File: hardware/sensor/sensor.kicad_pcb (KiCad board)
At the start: 2 copper layers, 25.7 x 45.5 mm, 49 parts, among them P1 CONN_01X05, SW1 Reset, T1 BUK9Y22, T2 DMP10H4D2s, U1 LMR16006, U2 OPA376AIDCK, U3 CD74HC4046, U5 Atmel_SAM_D09, X1 60V, X2 UART

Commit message: soo eigentlich gloub ke grossi änderige...
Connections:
- X2 pad : (no net) -> GND
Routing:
- net GND: track 92.3 -> 101.2 mm
- net (no net): track 0.00 -> 0.59 mm, vias 0 -> 1
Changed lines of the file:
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@@
   (general
     (links 157)
-    (no_connects 49)
-    (area 126.949999 54.051999 152.704001 99.618001)
+    (no_connects 47)
+    (area 122.153286 45.639999 152.704001 101.743)
     (thickness 1.6)
     (drawings 5)
-    (tracks 399)
+    (tracks 412)
     (zones 0)
     (modules 49)
@@
       (net 2 GND))
     (pad "" smd rect (at -4.425 0 90) (size 2.1 3) (layers B.Cu B.Paste B.Mask))
-    (pad "" smd rect (at 4.425 0 90) (size 2.1 3) (layers B.Cu B.Paste B.Mask))
+    (pad "" smd rect (at 4.425 0 90) (size 2.1 3) (layers B.Cu B.Paste B.Mask)
+      (net 2 GND))
   )
   (module LEDs:LED_0603 (layer B.Cu)
@@
   (gr_line (start 152.654 54.102) (end 152.654 99.568) (angle 90) (layer Edge.Cuts) (width 0.1))
   (gr_line (start 127 54.102) (end 152.654 54.102) (angle 90) (layer Edge.Cuts) (width 0.1))
+  (segment (start 146.292231 56.702127) (end 146.162289 56.572185) (width 0.4) (layer F.Cu) (net 0))
+  (segment (start 146.698298 56.702127) (end 146.292231 56.702127) (width 0.4) (layer F.Cu) (net 0))
+  (via (at 146.162289 56.572185) (size 1.3) (drill 0.9) (layers F.Cu B.Cu) (net 0))
   (segment (start 133.67004 65.024) (end 133.67004 63.52704) (width 0.4) (layer F.Cu) (net 1))
   (segment (start 133.67004 63.52704) (end 133.643 63.5) (width 0.4) (layer F.Cu) (net 1))
@@
   (segment (start 133.643 62.572) (end 134.62 61.595) (width 0.4) (layer F.Cu) (net 1))
   (segment (start 132.075 61.595) (end 134.62 61.595) (width 0.4) (layer F.Cu) (net 1))
+  (segment (start 131.944 74.676) (end 133.35 74.676) (width 0.4) (layer B.Cu) (net 2))
+  (segment (start 131.932 74.688) (end 131.944 74.676) (width 0.4) (layer B.Cu) (net 2))
+  (segment (start 131.932 75.488) (end 131.932 74.688) (width 0.4) (layer B.Cu) (net 2))
+  (segment (start 131.932 75.488) (end 132.538 75.488) (width 0.4) (layer B.Cu) (net 2))
+  (segment (start 131.932 75.488) (end 133.554 75.488) (width 0.4) (layer B.Cu) (net 2))
+  (via (at 134.366 74.676) (size 1.3) (drill 0.9) (layers F.Cu B.Cu) (net 2))
+  (segment (start 133.554 75.488) (end 134.366 74.676) (width 0.4) (layer B.Cu) (net 2))
+  (segment (start 139.167 81.026) (end 139.167 81.237011) (width 0.4) (layer B.Cu) (net 2))
+  (segment (start 139.167 81.237011) (end 138.196224 82.207787) (width 0.4) (layer B.Cu) (net 2))
+  (segment (start 138.196224 82.207787) (end 138.196224 82.45362) (width 0.4) (layer B.Cu) (net 2))
+  (segment (start 139.192 81.026) (end 139.192 81.282249) (width 0.25) (layer B.Cu) (net 2))
+  (segment (start 139.192 81.282249) (end 138.176 82.298249) (width 0.25) (layer B.Cu) (net 2))
+  (segment (start 138.176 82.298249) (end 138.176 82.667) (width 0.25) (layer B.Cu) (net 2))
   (segment (start 134.62 82.538) (end 134.378 82.538) (width 0.4) (layer B.Cu) (net 2))
   (segment (start 134.378 82.538) (end 133.604 83.312) (width 0.4) (layer B.Cu) (net 2))
@@
   (segment (start 129.54 56.515) (end 129.54 58.652966) (width 0.4) (layer B.Cu) (net 2))
   (segment (start 129.54 58.652966) (end 129.259483 58.933483) (width 0.4) (layer B.Cu) (net 2))
-  (segment (start 146.292231 56.702127) (end 146.162289 56.572185) (width 0.4) (layer F.Cu) (net 2))
-  (segment (start 146.698298 56.702127) (end 146.292231 56.702127) (width 0.4) (layer F.Cu) (net 2))
-  (via (at 146.162289 56.572185) (size 1.3) (drill 0.9) (layers F.Cu B.Cu) (net 2))
   (segment (start 139.434 87.63) (end 141.224 87.63) (width 0.25) (layer B.Cu) (net 2))
   (segment (start 141.224 87.63) (end 141.732 88.138) (width 0.25) (layer B.Cu) (net 2))
@@
   (segment (start 129.54 60.96) (end 130.175 61.595) (width 0.25) (layer F.Cu) (net 12))
   (segment (start 131.509 63.524) (end 131.533 63.5) (width 0.25) (layer F.Cu) (net 12))
+  (segment (start 140.966 79.166) (end 140.966 81.339312) (width 0.25) (layer B.Cu) (net 13))
+  (segment (start 140.099479 83.250624) (end 141.006852 84.157997) (width 0.25) (layer B.Cu) (net 13))
+  (segment (start 140.966 81.339312) (end 140.099479 82.205833) (width 0.25) (layer B.Cu) (net 13))
+  (segment (start 140.099479 82.205833) (end 140.099479 83.250624) (width 0.25) (layer B.Cu) (net 13))
+  (segment (start 141.006852 84.157997) (end 143.593997 84.157997) (width 0.25) (layer B.Cu) (net 13))
   (segment (start 150.528775 61.582876) (end 150.528775 62.502114) (width 0.4) (layer F.Cu) (net 13))
+  (segment (start 143.523001 84.157997) (end 147.006931 80.674067) (width 0.3) (layer B.Cu) (net 13))
+  (via (at 150.528775 62.502114) (size 1.3) (drill 0.9) (layers F.Cu B.Cu) (net 13))
+  (segment (start 147.006931 80.674067) (end 150.528775 77.152223) (width 0.3) (layer B.Cu) (net 13))
+  (segment (start 150.528775 77.152223) (end 150.528775 63.421352) (width 0.3) (layer B.Cu) (net 13))
+  (segment (start 150.528775 59.696775) (end 150.528775 61.582876) (width 0.4) (layer F.Cu) (net 13))
+  (segment (start 150.528775 63.421352) (end 150.528775 62.502114) (width 0.3) (layer B.Cu) (net 13))
+  (segment (start 149.086 57.404) (end 149.086 58.254) (width 0.4) (layer F.Cu) (net 13))
   (segment (start 149.086 58.254) (end 150.528775 59.696775) (width 0.4) (layer F.Cu) (net 13))
-  (segment (start 149.086 57.404) (end 149.086 58.254) (width 0.4) (layer F.Cu) (net 13))
-  (segment (start 150.528775 63.421352) (end 150.528775 62.502114) (width 0.3) (layer B.Cu) (net 13))
-  (segment (start 150.528775 59.696775) (end 150.528775 61.582876) (width 0.4) (layer F.Cu) (net 13))
-  (segment (start 150.528775 77.152223) (end 150.528775 63.421352) (width 0.3) (layer B.Cu) (net 13))
-  (segment (start 147.006931 80.674067) (end 150.528775 77.152223) (width 0.3) (layer B.Cu) (net 13))
-  (via (at 150.528775 62.502114) (size 1.3) (drill 0.9) (layers F.Cu B.Cu) (net 13))
   (segment (start 145.542 88.646) (end 145.542 91.036) (width 0.4) (layer F.Cu) (net 13))
   (segment (start 145.542 91.036) (end 145.535 91.043) (width 0.4) (layer F.Cu) (net 13))
@@
   (segment (start 145.542 86.106) (end 145.542 88.646) (width 0.4) (layer B.Cu) (net 13))
   (via (at 145.542 88.646) (size 1.3) (drill 0.9) (layers F.Cu B.Cu) (net 13))
-  (segment (start 143.523001 84.157997) (end 143.593997 84.157997) (width 0.4) (layer B.Cu) (net 13))
-  (segment (start 143.523001 84.157997) (end 147.006931 80.674067) (width 0.3) (layer B.Cu) (net 13))
-  (segment (start 140.966 79.166) (end 140.966 81.418762) (width 0.3) (layer B.Cu) (net 13))
-  (segment (start 139.683853 82.700909) (end 141.14094 84.157997) (width 0.3) (layer B.Cu) (net 13))
-  (segment (start 140.966 81.418762) (end 139.683853 82.700909) (width 0.3) (layer B.Cu) (net 13))
-  (segment (start 141.14094 84.157997) (end 143.523001 84.157997) (width 0.3) (layer B.Cu) (net 13))
   (segment (start 134.62 65.024) (end 134.62 64.99) (width 0.4) (layer F.Cu) (net 14))
   (segment (start 134.62 64.99) (end 135.094 64.516) (width 0.4) (layer F.Cu) (net 14))
@@
   (segment (start 143.764 57.912) (end 143.256 57.912) (width 0.25) (layer F.Cu) (net 18))
   (segment (start 143.256 57.912) (end 142.24 58.928) (width 0.25) (layer F.Cu) (net 18))
-  (segment (start 140.466 79.166) (end 140.466 81.017357) (width 0.25) (layer B.Cu) (net 19))
-  (segment (start 140.466 81.017357) (end 138.948786 82.534571) (width 0.25) (layer B.Cu) (net 19))
-  (segment (start 139.735427 94.996) (end 138.733 94.996) (width 0.25) (layer B.Cu) (net 19))
-  (segment (start 138.948786 82.534571) (end 138.948786 83.194299) (width 0.25) (layer B.Cu) (net 19))
-  (segment (start 143.224212 87.469826) (end 143.224212 88.662786) (width 0.25) (layer B.Cu) (net 19))
-  (segment (start 138.948786 83.194299) (end 142.521474 86.766987) (width 0.25) (layer B.Cu) (net 19))
-  (segment (start 142.521474 86.766987) (end 142.521474 86.767088) (width 0.25) (layer B.Cu) (net 19))
+  (segment (start 140.466 79.166) (end 140.466 81.101811) (width 0.25) (layer B.Cu) (net 19))
+  (segment (start 140.466 81.101811) (end 139.460312 82.107499) (width 0.25) (layer B.Cu) (net 19))
+  (segment (start 139.460312 82.107499) (end 139.460312 83.705825) (width 0.25) (layer B.Cu) (net 19))
+  (segment (start 138.733 94.996) (end 137.59 93.853) (width 0.25) (layer B.Cu) (net 19))
+  (segment (start 139.460312 83.705825) (end 142.521474 86.766987) (width 0.25) (layer B.Cu) (net 19))
   (segment (start 142.521474 86.767088) (end 143.224212 87.469826) (width 0.25) (layer B.Cu) (net 19))
   (segment (start 143.224212 88.662786) (end 141.951999 89.934999) (width 0.25) (layer B.Cu) (net 19))
+  (segment (start 141.951999 92.779428) (end 139.735427 94.996) (width 0.25) (layer B.Cu) (net 19))
+  (segment (start 142.521474 86.766987) (end 142.521474 86.767088) (width 0.25) (layer B.Cu) (net 19))
+  (segment (start 137.59 93.853) (end 137.565 93.853) (width 0.25) (layer B.Cu) (net 19))
+  (segment (start 143.224212 87.469826) (end 143.224212 88.662786) (width 0.25) (layer B.Cu) (net 19))
   (segment (start 141.951999 89.934999) (end 141.951999 92.779428) (width 0.25) (layer B.Cu) (net 19))
-  (segment (start 141.951999 92.779428) (end 139.735427 94.996) (width 0.25) (layer B.Cu) (net 19))
-  (segment (start 138.733 94.996) (end 137.59 93.853) (width 0.25) (layer B.Cu) (net 19))
-  (segment (start 137.59 93.853) (end 137.565 93.853) (width 0.25) (layer B.Cu) (net 19))
+  (segment (start 139.735427 94.996) (end 138.733 94.996) (width 0.25) (layer B.Cu) (net 19))
   (segment (start 136.271 93.98) (end 137.438 93.98) (width 0.4) (layer B.Cu) (net 19))
   (segment (start 137.438 93.98) (end 137.565 93.853) (width 0.4) (layer B.Cu) (net 19))
@@
     (min_thickness 0.254)
     (keepout (tracks not_allowed) (vias not_allowed) (copperpour not_allowed))
-    (fill yes (arc_segments 16) (thermal_gap 0.508) (thermal_bridge_width 0.508))
+    (fill (arc_segments 16) (thermal_gap 0.508) (thermal_bridge_width 0.508))
     (polygon
       (pts
-        (xy 127.381 74.295) (xy 130.683 74.295) (xy 130.683 80.264) (xy 127.381 80.264)
+        (xy 127.381 74.295) (xy 130.937 74.295) (xy 130.937 80.264) (xy 127.381 80.264)
       )
     )

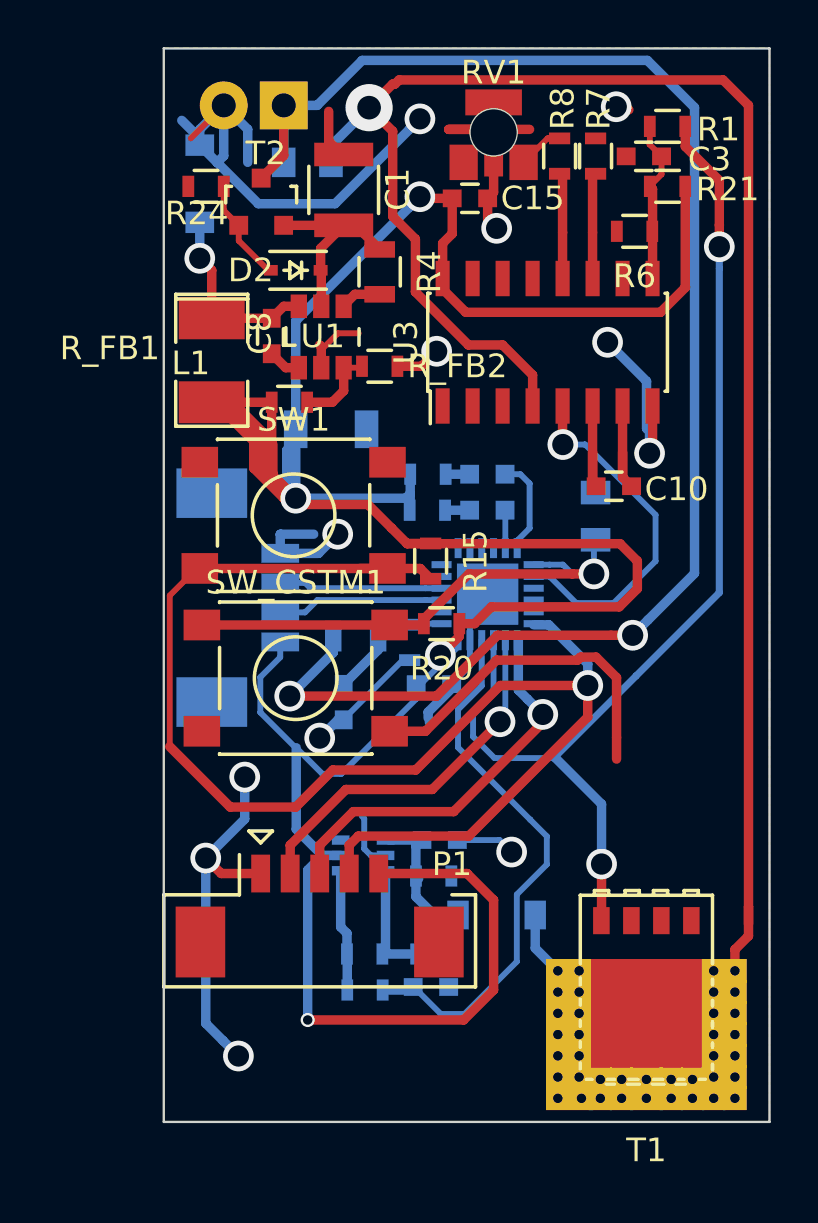
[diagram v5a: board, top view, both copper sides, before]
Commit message: Sensor fixes
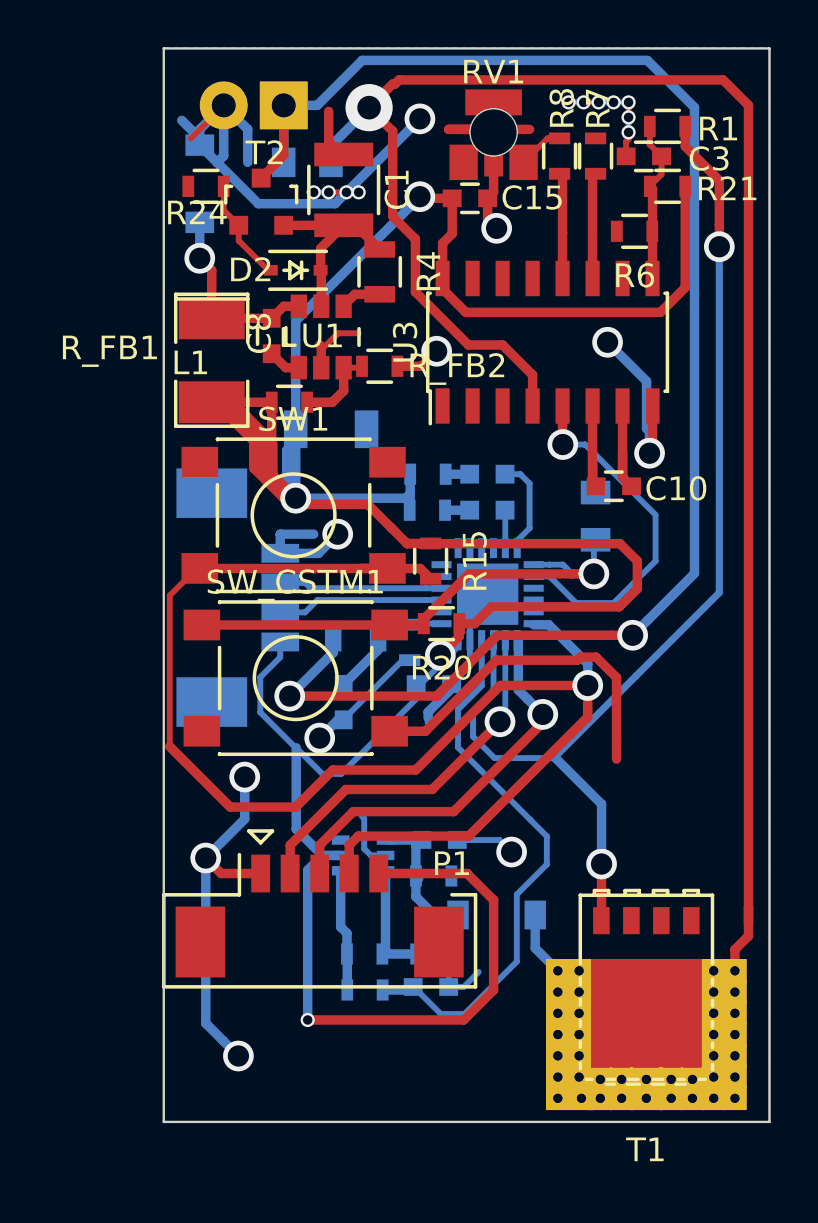
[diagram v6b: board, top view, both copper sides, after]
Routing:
- net GND: track 101.2 -> 110.9 mm, vias 11 -> 22
- net (no net): track 0.59 -> 0.00 mm, vias 1 -> 0
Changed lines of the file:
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@@
-(kicad_pcb (version 4) (host pcbnew "(2015-09-15 BZR 6201)-product")
+(kicad_pcb (version 4) (host pcbnew 4.0.2-stable)
   (general
-    (links 157)
-    (no_connects 47)
+    (links 158)
+    (no_connects 43)
     (area 122.153286 45.639999 152.704001 101.743)
     (thickness 1.6)
     (drawings 5)
-    (tracks 412)
+    (tracks 438)
     (zones 0)
     (modules 49)
@@
   )
   (setup
-    (last_trace_width 0.4)
+    (last_trace_width 0.25)
     (user_trace_width 0.4)
     (trace_clearance 0.2)
@@
     (aux_axis_origin 0 0)
     (grid_origin 127 99.568)
-    (visible_elements FFFFFF7F)
+    (visible_elements 7FFFFFFF)
     (pcbplotparams
-      (layerselection 0x01000_80000001)
+      (layerselection 0x010f0_80000001)
       (usegerberextensions false)
       (excludeedgelayer true)
@@
   (gr_line (start 152.654 54.102) (end 152.654 99.568) (angle 90) (layer Edge.Cuts) (width 0.1))
   (gr_line (start 127 54.102) (end 152.654 54.102) (angle 90) (layer Edge.Cuts) (width 0.1))
-  (segment (start 146.292231 56.702127) (end 146.162289 56.572185) (width 0.4) (layer F.Cu) (net 0))
-  (segment (start 146.698298 56.702127) (end 146.292231 56.702127) (width 0.4) (layer F.Cu) (net 0))
-  (via (at 146.162289 56.572185) (size 1.3) (drill 0.9) (layers F.Cu B.Cu) (net 0))
   (segment (start 133.67004 65.024) (end 133.67004 63.52704) (width 0.4) (layer F.Cu) (net 1))
   (segment (start 133.67004 63.52704) (end 133.643 63.5) (width 0.4) (layer F.Cu) (net 1))
@@
   (segment (start 133.643 62.572) (end 134.62 61.595) (width 0.4) (layer F.Cu) (net 1))
   (segment (start 132.075 61.595) (end 134.62 61.595) (width 0.4) (layer F.Cu) (net 1))
+  (segment (start 134.736426 60.198) (end 135.255 60.198) (width 0.25) (layer B.Cu) (net 2))
+  (via (at 135.255 60.198) (size 0.6) (drill 0.4) (layers F.Cu B.Cu) (net 2))
+  (via (at 133.35 60.198) (size 0.6) (drill 0.4) (layers F.Cu B.Cu) (net 2))
+  (segment (start 133.985 60.198) (end 133.35 60.198) (width 0.25) (layer B.Cu) (net 2))
+  (segment (start 134.736426 60.198) (end 133.985 60.198) (width 0.25) (layer F.Cu) (net 2))
+  (via (at 133.985 60.198) (size 0.6) (drill 0.4) (layers F.Cu B.Cu) (net 2))
+  (segment (start 134.736426 60.198) (end 137.397864 57.536562) (width 0.4) (layer B.Cu) (net 2))
+  (via (at 134.736426 60.198) (size 0.6) (drill 0.4) (layers F.Cu B.Cu) (net 2))
+  (segment (start 134.254483 60.679943) (end 134.736426 60.198) (width 0.4) (layer B.Cu) (net 2))
+  (segment (start 139.7 93.853) (end 140.335 93.218) (width 0.25) (layer B.Cu) (net 2))
+  (segment (start 139.09 93.853) (end 139.7 93.853) (width 0.25) (layer B.Cu) (net 2))
+  (segment (start 139.065 93.853) (end 139.09 93.853) (width 0.25) (layer B.Cu) (net 2))
+  (segment (start 139.065 93.853) (end 139.065 92.583) (width 0.25) (layer B.Cu) (net 2))
+  (segment (start 139.065 92.583) (end 139.192 92.456) (width 0.25) (layer B.Cu) (net 2))
+  (segment (start 144.78 56.388) (end 144.145 56.388) (width 0.25) (layer B.Cu) (net 2))
+  (via (at 144.145 56.388) (size 0.6) (drill 0.4) (layers F.Cu B.Cu) (net 2))
+  (segment (start 145.415 56.388) (end 144.78 56.388) (width 0.25) (layer F.Cu) (net 2))
+  (via (at 144.78 56.388) (size 0.6) (drill 0.4) (layers F.Cu B.Cu) (net 2))
+  (segment (start 146.05 56.388) (end 145.415 56.388) (width 0.25) (layer B.Cu) (net 2))
+  (via (at 145.415 56.388) (size 0.6) (drill 0.4) (layers F.Cu B.Cu) (net 2))
+  (via (at 146.05 56.388) (size 0.6) (drill 0.4) (layers F.Cu B.Cu) (net 2))
+  (segment (start 146.685 56.388) (end 146.05 56.388) (width 0.25) (layer B.Cu) (net 2))
+  (segment (start 146.685 57.023) (end 146.685 56.388) (width 0.25) (layer F.Cu) (net 2))
+  (via (at 146.685 56.388) (size 0.6) (drill 0.4) (layers F.Cu B.Cu) (net 2))
+  (via (at 146.685 57.023) (size 0.6) (drill 0.4) (layers F.Cu B.Cu) (net 2))
+  (segment (start 146.685 57.658) (end 146.685 57.023) (width 0.25) (layer B.Cu) (net 2))
+  (segment (start 146.685 57.946) (end 146.685 57.658) (width 0.25) (layer F.Cu) (net 2))
+  (via (at 146.685 57.658) (size 0.6) (drill 0.4) (layers F.Cu B.Cu) (net 2))
+  (segment (start 146.582 58.674) (end 146.582 58.049) (width 0.25) (layer F.Cu) (net 2))
+  (segment (start 146.582 58.049) (end 146.685 57.946) (width 0.25) (layer F.Cu) (net 2))
   (segment (start 131.944 74.676) (end 133.35 74.676) (width 0.4) (layer B.Cu) (net 2))
   (segment (start 131.932 74.688) (end 131.944 74.676) (width 0.4) (layer B.Cu) (net 2))
@@
   (segment (start 140.97 60.198) (end 140.716 60.452) (width 0.4) (layer F.Cu) (net 2))
   (segment (start 131.005943 60.679943) (end 134.254483 60.679943) (width 0.4) (layer B.Cu) (net 2))
-  (segment (start 134.254483 60.679943) (end 137.397864 57.536562) (width 0.4) (layer B.Cu) (net 2))
   (segment (start 137.397864 57.536562) (end 137.847863 57.086563) (width 0.4) (layer B.Cu) (net 2))
   (via (at 137.847863 57.086563) (size 1.3) (drill 0.9) (layers F.Cu B.Cu) (net 2))
@@
     (min_thickness 0.254)
     (keepout (tracks not_allowed) (vias not_allowed) (copperpour not_allowed))
-    (fill (arc_segments 16) (thermal_gap 0.508) (thermal_bridge_width 0.508))
+    (fill yes (arc_segments 16) (thermal_gap 0.508) (thermal_bridge_width 0.508))
     (polygon
       (pts
